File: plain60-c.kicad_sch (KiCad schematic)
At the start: 175 parts, among them J1 HRO-TYPE-C-31-M-12, J2 ISP, J3 ai03_ud, K1 KEYSW, K10 KEYSW, K11 KEYSW, K12 KEYSW, K13 KEYSW, K14 KEYSW, K15 KEYSW, K15-1 KEYSW, K16 KEYSW, K17 KEYSW, K18 KEYSW, K19 KEYSW, K2 KEYSW, K20 KEYSW, K21 KEYSW, K22 KEYSW, K23 KEYSW, K24 KEYSW, K25 KEYSW, K26 KEYSW, K27 KEYSW, K28 KEYSW, K29 KEYSW, K3 KEYSW, K31 KEYSW, K31-1 KEYSW, K32 KEYSW, K33 KEYSW, K34 KEYSW, K35 KEYSW, K36 KEYSW, K37 KEYSW, K38 KEYSW, K39 KEYSW, K4 KEYSW, K40 KEYSW, K41 KEYSW, K42 KEYSW, K43 KEYSW, K44 KEYSW, K44-1 KEYSW, K46 KEYSW, K46-1 KEYSW, K47 KEYSW, K48 KEYSW, K49 KEYSW, K5 KEYSW, K50 KEYSW, K51 KEYSW, K52 KEYSW, K53 KEYSW, K54 KEYSW, K55 KEYSW, K56 KEYSW, K57 KEYSW, K58 KEYSW, K58-1 KEYSW, K59 KEYSW, K6 KEYSW, K61 KEYSW, K61-1 KEYSW, K62 KEYSW, K62-1 KEYSW, K63 KEYSW, K63-1 KEYSW, K67 KEYSW, K67-1 KEYSW, K7 KEYSW, K71 KEYSW, K72 KEYSW, K72-1 KEYSW, K73 KEYSW, K73-1 KEYSW, K74 KEYSW, K74-1 KEYSW, K8 KEYSW, K9 KEYSW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

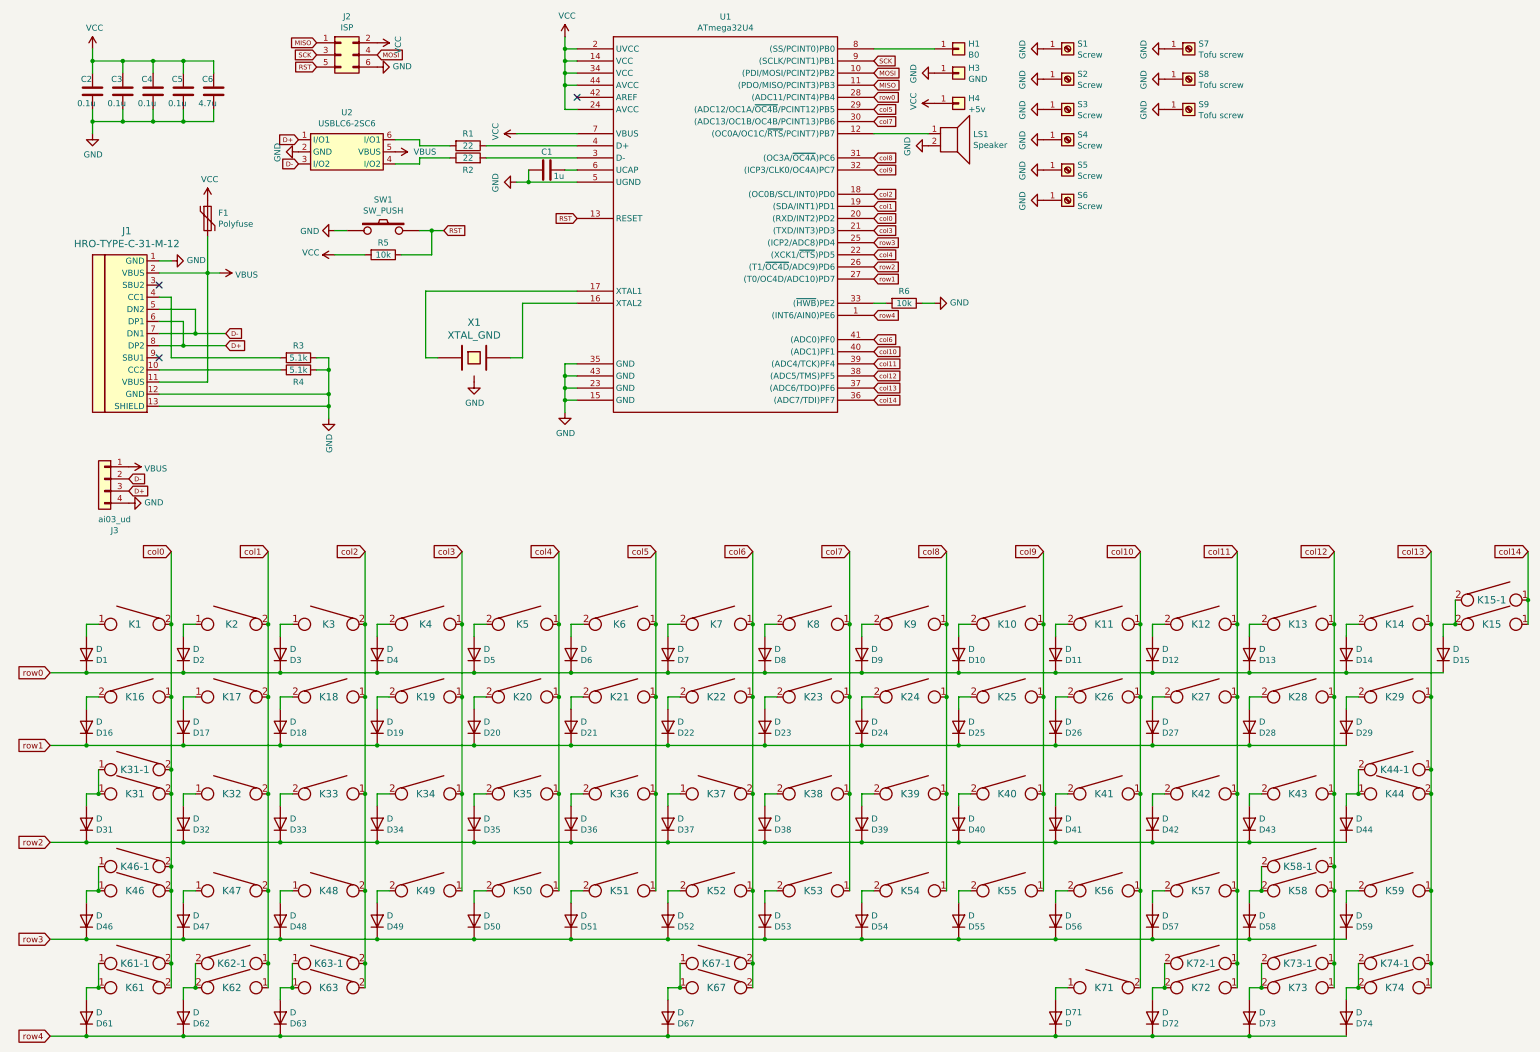
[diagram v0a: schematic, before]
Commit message: remove usb-c and add back silkscreen
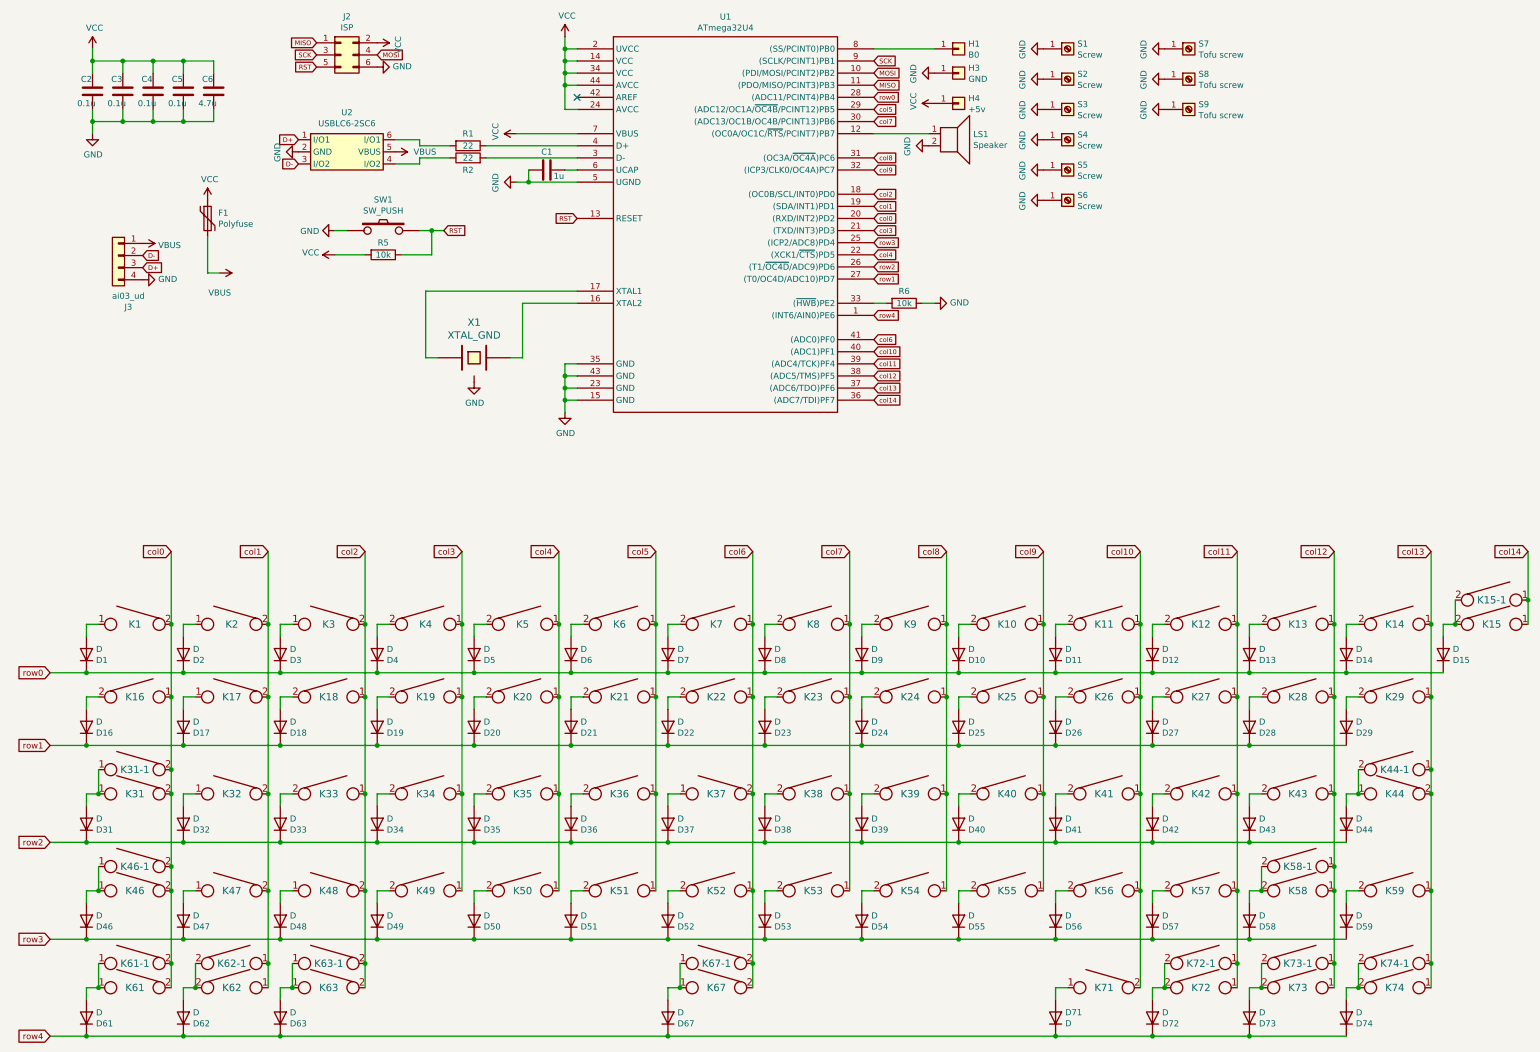
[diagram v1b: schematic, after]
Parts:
- removed J1: HRO-TYPE-C-31-M-12, Keeb_components:HRO-TYPE-C-31-M-12, symbol Type-C:HRO-TYPE-C-31-M-12
- removed R3, R4: 5.1k, Keeb_components:R_0805, symbol Device:R
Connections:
- no-connect marks 3 -> 1
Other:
- moved on the sheet: J3

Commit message: changed silk, removed poker mounts
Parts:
- removed LS1: Speaker, Keeb_components:speaker_AST1109MLTRQ, symbol Device:Speaker
- removed S7, S8, S9: Tofu screw, footprints:5.5_5x2.5mm, symbol Connector:Screw_Terminal_01x01
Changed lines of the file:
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@@
     (stroke (width 0) (type solid) (color 0 0 0 0))
   )
-  (wire (pts (xy 194.31 43.18) (xy 205.74 43.18))
-    (stroke (width 0) (type solid) (color 0 0 0 0))
-  )
   (wire (pts (xy 196.85 78.74) (xy 194.31 78.74))
     (stroke (width 0) (type solid) (color 0 0 0 0))
@@
     )
   )
-  (symbol (lib_id "Power:GND") (at 205.74 45.72 270) (unit 1)
-    (in_bom yes) (on_board yes)
-    (property "Reference" "#PWR0132" (id 0) (at 199.39 45.72 0)
-      (effects (font (size 1.27 1.27)) hide)
-    )
-    (property "Value" "GND" (id 1) (at 201.3458 45.847 0))
-    (property "Footprint" "" (id 2) (at 205.74 45.72 0)
-      (effects (font (size 1.27 1.27)) hide)
-    )
-    (property "Datasheet" "" (id 3) (at 205.74 45.72 0)
-      (effects (font (size 1.27 1.27)) hide)
-    )
-  )
   (symbol (lib_id "Power:GND") (at 207.01 30.48 270) (unit 1)
     (in_bom yes) (on_board yes)
@@
     )
   )
-  (symbol (lib_id "Power:GND") (at 255.27 25.4 270) (unit 1)
-    (in_bom yes) (on_board yes)
-    (property "Reference" "#PWR0127" (id 0) (at 248.92 25.4 0)
-      (effects (font (size 1.27 1.27)) hide)
-    )
-    (property "Value" "GND" (id 1) (at 250.8758 25.527 0))
-    (property "Footprint" "" (id 2) (at 255.27 25.4 0)
-      (effects (font (size 1.27 1.27)) hide)
-    )
-    (property "Datasheet" "" (id 3) (at 255.27 25.4 0)
-      (effects (font (size 1.27 1.27)) hide)
-    )
-  )
-  (symbol (lib_id "Power:GND") (at 255.27 31.75 270) (unit 1)
-    (in_bom yes) (on_board yes)
-    (property "Reference" "#PWR0128" (id 0) (at 248.92 31.75 0)
-      (effects (font (size 1.27 1.27)) hide)
-    )
-    (property "Value" "GND" (id 1) (at 250.8758 31.877 0))
-    (property "Footprint" "" (id 2) (at 255.27 31.75 0)
-      (effects (font (size 1.27 1.27)) hide)
-    )
-    (property "Datasheet" "" (id 3) (at 255.27 31.75 0)
-      (effects (font (size 1.27 1.27)) hide)
-    )
-  )
-  (symbol (lib_id "Power:GND") (at 255.27 38.1 270) (unit 1)
-    (in_bom yes) (on_board yes)
-    (property "Reference" "#PWR0129" (id 0) (at 248.92 38.1 0)
-      (effects (font (size 1.27 1.27)) hide)
-    )
-    (property "Value" "GND" (id 1) (at 250.8758 38.227 0))
-    (property "Footprint" "" (id 2) (at 255.27 38.1 0)
-      (effects (font (size 1.27 1.27)) hide)
-    )
-    (property "Datasheet" "" (id 3) (at 255.27 38.1 0)
-      (effects (font (size 1.27 1.27)) hide)
-    )
-  )
   (symbol (lib_id "Device:R") (at 91.44 68.58 270) (unit 1)
     (in_bom yes) (on_board yes)
@@
     )
   )
-  (symbol (lib_id "Connector:Screw_Terminal_01x01") (at 260.35 25.4 0) (unit 1)
-    (in_bom yes) (on_board yes)
-    (property "Reference" "S7" (id 0) (at 262.382 24.3332 0)
-      (effects (font (size 1.27 1.27)) (justify left))
-    )
-    (property "Value" "Tofu screw" (id 1) (at 262.382 26.6446 0)
-      (effects (font (size 1.27 1.27)) (justify left))
-    )
-    (property "Footprint" "footprints:5.5_5x2.5mm" (id 2) (at 260.35 25.4 0)
-      (effects (font (size 1.27 1.27)) hide)
-    )
-    (property "Datasheet" "~" (id 3) (at 260.35 25.4 0)
-      (effects (font (size 1.27 1.27)) hide)
-    )
-  )
-  (symbol (lib_id "Connector:Screw_Terminal_01x01") (at 260.35 31.75 0) (unit 1)
-    (in_bom yes) (on_board yes)
-    (property "Reference" "S8" (id 0) (at 262.382 30.6832 0)
-      (effects (font (size 1.27 1.27)) (justify left))
-    )
-    (property "Value" "Tofu screw" (id 1) (at 262.382 32.9946 0)
-      (effects (font (size 1.27 1.27)) (justify left))
-    )
-    (property "Footprint" "footprints:5.5_5x2.5mm" (id 2) (at 260.35 31.75 0)
-      (effects (font (size 1.27 1.27)) hide)
-    )
-    (property "Datasheet" "~" (id 3) (at 260.35 31.75 0)
-      (effects (font (size 1.27 1.27)) hide)
-    )
-  )
-  (symbol (lib_id "Connector:Screw_Terminal_01x01") (at 260.35 38.1 0) (unit 1)
-    (in_bom yes) (on_board yes)
-    (property "Reference" "S9" (id 0) (at 262.382 37.0332 0)
-      (effects (font (size 1.27 1.27)) (justify left))
-    )
-    (property "Value" "Tofu screw" (id 1) (at 262.382 39.3446 0)
-      (effects (font (size 1.27 1.27)) (justify left))
-    )
-    (property "Footprint" "footprints:5.5_5x2.5mm" (id 2) (at 260.35 38.1 0)
-      (effects (font (size 1.27 1.27)) hide)
-    )
-    (property "Datasheet" "~" (id 3) (at 260.35 38.1 0)
-      (effects (font (size 1.27 1.27)) hide)
-    )
-  )
   (symbol (lib_id "Device:D") (at 29.21 152.4 270) (mirror x) (unit 1)
     (in_bom yes) (on_board yes)
@@
     )
   )
-  (symbol (lib_id "Device:Speaker") (at 210.82 43.18 0) (unit 1)
-    (in_bom yes) (on_board yes)
-    (property "Reference" "LS1" (id 0) (at 215.138 43.307 0)
-      (effects (font (size 1.27 1.27)) (justify left))
-    )
-    (property "Value" "Speaker" (id 1) (at 215.138 45.593 0)
-      (effects (font (size 1.27 1.27)) (justify left))
-    )
-    (property "Footprint" "Keeb_components:speaker_AST1109MLTRQ" (id 2) (at 210.82 48.26 0)
-      (effects (font (size 1.27 1.27)) hide)
-    )
-    (property "Datasheet" "~" (id 3) (at 210.566 44.45 0)
-      (effects (font (size 1.27 1.27)) hide)
-    )
-  )
   (symbol (lib_id "Connector_Generic:Conn_02x03_Odd_Even") (at 82.55 26.67 0) (unit 1)
     (in_bom yes) (on_board yes)
@@
       (reference "#PWR0126") (unit 1) (value "GND") (footprint "")
     )
-    (path "/00000000-0000-0000-0000-00005c59e1d1"
-      (reference "#PWR0127") (unit 1) (value "GND") (footprint "")
-    )
-    (path "/00000000-0000-0000-0000-00005c5ea792"
-      (reference "#PWR0128") (unit 1) (value "GND") (footprint "")
-    )
-    (path "/00000000-0000-0000-0000-00005c610569"
-      (reference "#PWR0129") (unit 1) (value "GND") (footprint "")
-    )
     (path "/00000000-0000-0000-0000-00005d8f6178"
       (reference "#PWR0130") (unit 1) (value "VBUS") (footprint "")
@@
       (reference "#PWR0131") (unit 1) (value "GND") (footprint "")
     )
-    (path "/00000000-0000-0000-0000-00005e0cf144"
-      (reference "#PWR0132") (unit 1) (value "GND") (footprint "")
-    )
     (path "/00000000-0000-0000-0000-00005c2b0975"
       (reference "C1") (unit 1) (value "1u") (footprint "Keeb_components:C_0805")
@@
       (reference "K74-1") (unit 1) (value "KEYSW") (footprint "Keeb_switches:CHERRY_PLATE_150H")
     )
-    (path "/00000000-0000-0000-0000-00005e0cbbd2"
-      (reference "LS1") (unit 1) (value "Speaker") (footprint "Keeb_components:speaker_AST1109MLTRQ")
-    )
     (path "/00000000-0000-0000-0000-00005c29eea3"
       (reference "R1") (unit 1) (value "22") (footprint "Keeb_components:R_0805")
@@
       (reference "S6") (unit 1) (value "Screw") (footprint "footprints:5.5_5x2.5mm")
     )
-    (path "/00000000-0000-0000-0000-00005c59e1cb"
-      (reference "S7") (unit 1) (value "Tofu screw") (footprint "footprints:5.5_5x2.5mm")
-    )
-    (path "/00000000-0000-0000-0000-00005c5ea78c"
-      (reference "S8") (unit 1) (value "Tofu screw") (footprint "footprints:5.5_5x2.5mm")
-    )
-    (path "/00000000-0000-0000-0000-00005c610563"
-      (reference "S9") (unit 1) (value "Tofu screw") (footprint "footprints:5.5_5x2.5mm")
-    )
     (path "/00000000-0000-0000-0000-00005c2a2ecd"
